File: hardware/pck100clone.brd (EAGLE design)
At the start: 85.7 x 68.6 mm, 222 parts, among them IC1 LM358N, IC3 LM358N, IC4 LM358N, IC5 LM358N, Q1 2SC945, Q2 2SC945, Q3 2N3906, Q4 2N3906, Q5 2N3904, Q6 2N3904

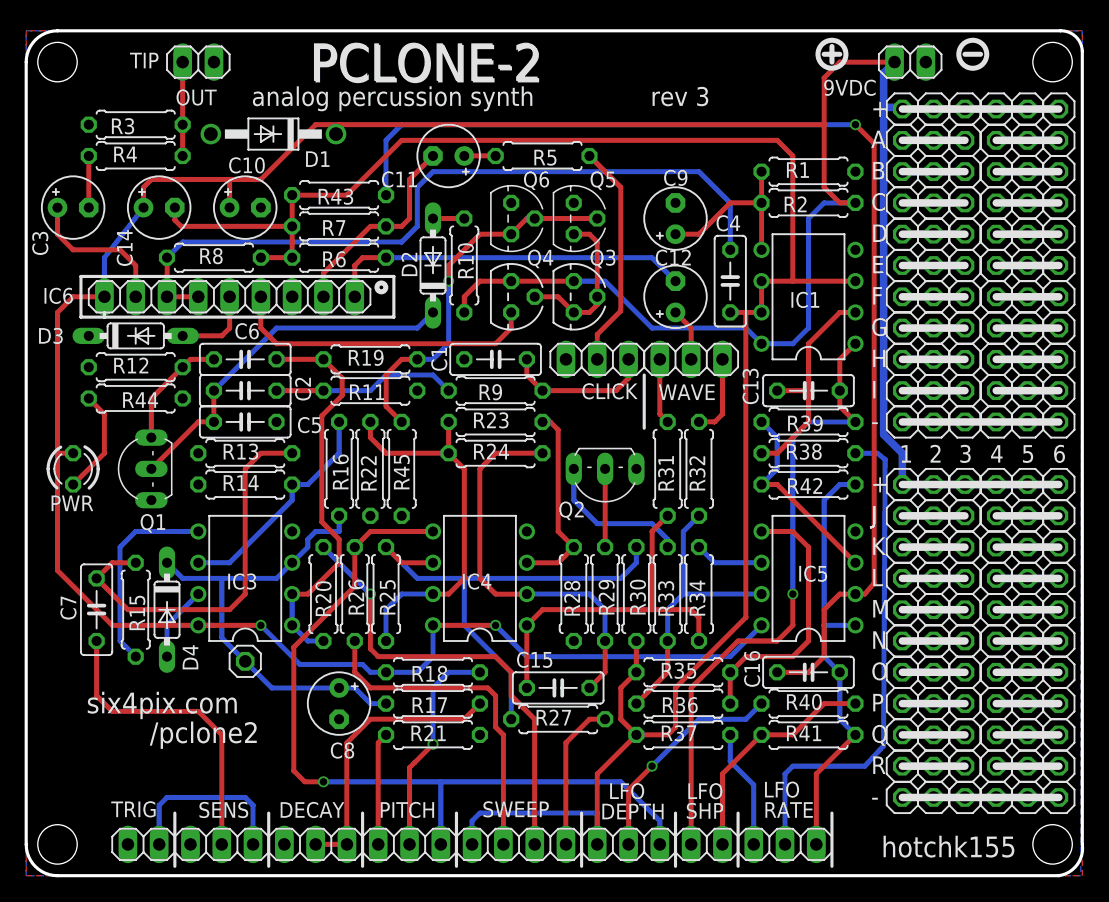
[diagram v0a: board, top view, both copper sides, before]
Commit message: REV4
add vca input trim / add series polarity diode
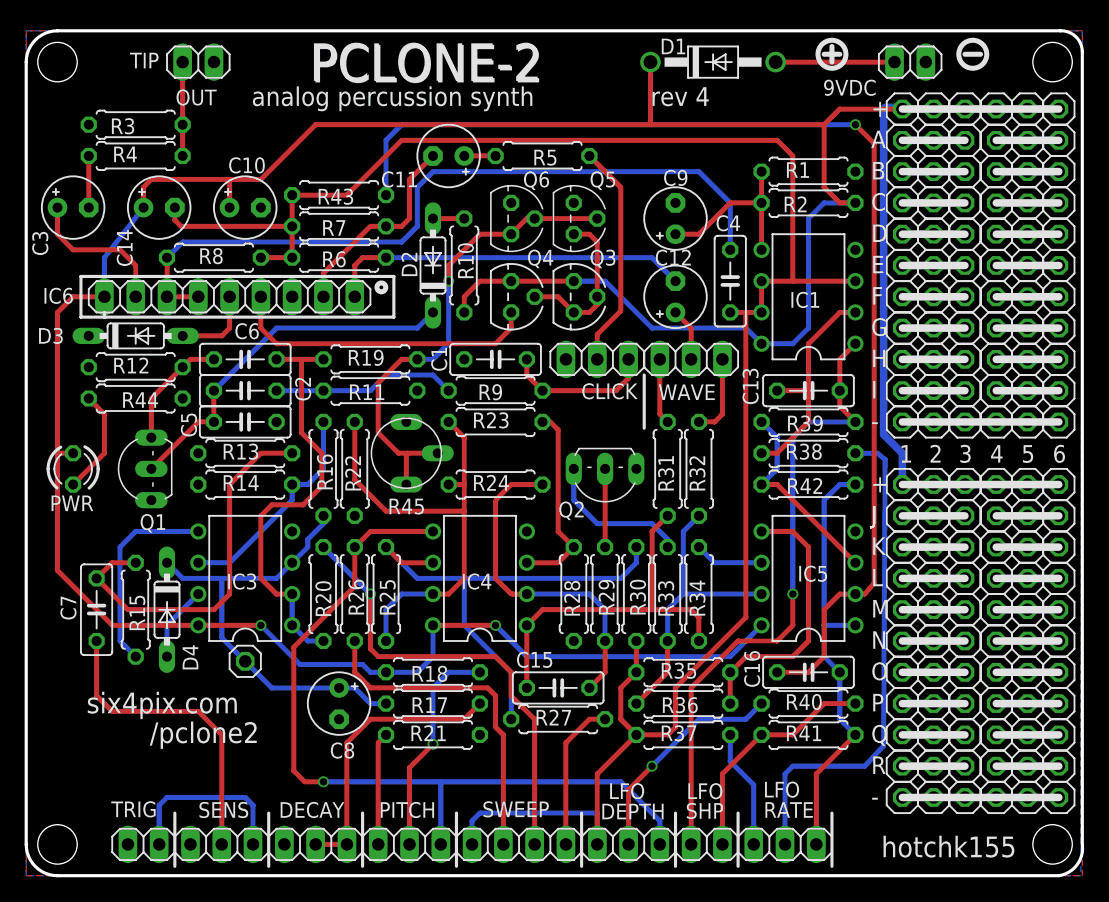
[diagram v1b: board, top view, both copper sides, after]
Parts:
- R45: value 4k7 -> 10k; device rcl:0207/7 -> jason_eagle6:TRIM-N
- moved D1 36.2 mm to (64.6, 67.3), turned to 0 degrees
- moved R24 2.54 mm to (47.0, 33.0)
- moved R45 1.33 mm to (39.8, 35.6), turned to 180 degrees
- moved R16 1.27 mm to (33.0, 34.3)
- moved R22 1.27 mm to (35.6, 34.3)
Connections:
- new net N$2: 9VDC.1, D1.A
- net BA662_1: now also R45.B, R45.W; no longer R45.1
- net GND: now also R45.A; no longer D1.A, R45.2
- net VCC: no longer 9VDC.1
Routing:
- net N$2: track 0.00 -> 9.65 mm
- net BA662_1: track 30.5 -> 39.2 mm
- net N$32: track 31.3 -> 39.1 mm
- net N$34: track 32.6 -> 27.5 mm
- net VCC: track 290.2 -> 287.2 mm
- net TRIGGER: track 32.7 -> 34.5 mm
- net N$8: track 38.1 -> 36.4 mm
- net N$4: track 31.8 -> 31.1 mm
- net N$6: track 18.4 -> 17.9 mm
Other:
- board text added: "rev 4"
- board text removed: "rev 3"
